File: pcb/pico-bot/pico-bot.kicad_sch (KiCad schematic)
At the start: 2 parts

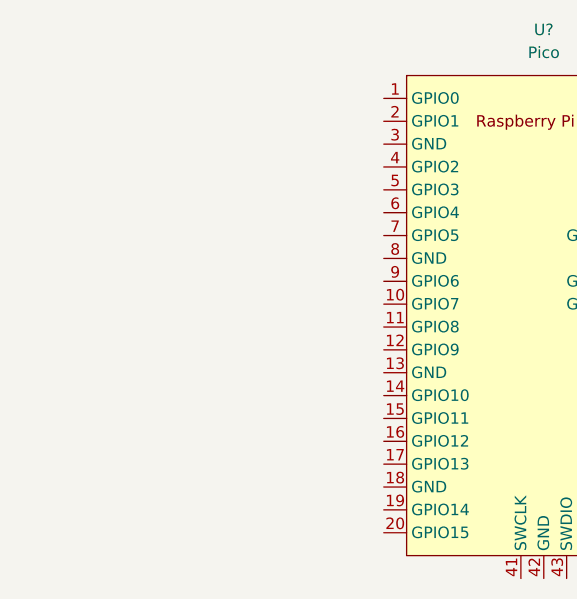
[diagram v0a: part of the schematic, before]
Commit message: Add tb6612fng and mpu6050
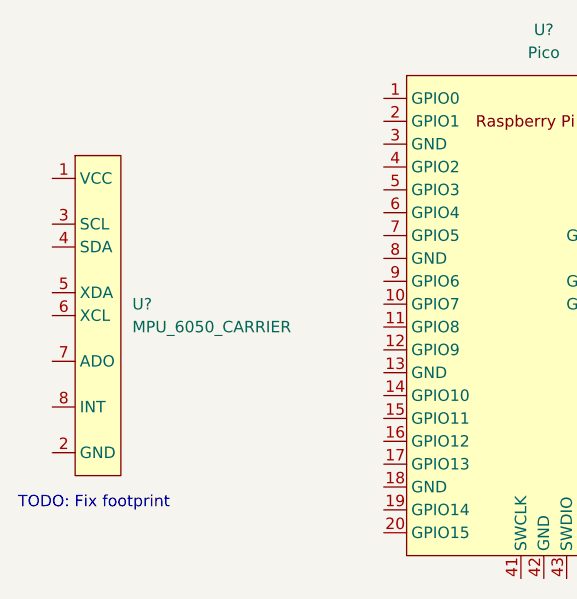
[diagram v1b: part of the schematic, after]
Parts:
- added U?: MPU_6050_CARRIER, symbol pico-bot:MPU_6050_CARRIER
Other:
- note added: "TODO: Fix footprint"
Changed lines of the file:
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@@
 (kicad_sch (version 20211123) (generator eeschema)
   (paper "A4")
+  (text "TODO: Fix footprint" (at 96.52 123.19 0)
+    (effects (font (size 1.27 1.27)) (justify left bottom))
+  )
   (symbol (lib_id "pico-bot:TB6612FNG_DUAL_MOTOR_CARRIER") (at 205.74 87.63 0) (unit 1)
     (in_bom yes) (on_board yes) (fields_autoplaced)
@@
     (pin "8")
     (pin "9")
+  )
+  (symbol (lib_id "pico-bot:MPU_6050_CARRIER") (at 102.87 83.82 0) (unit 1)
+    (in_bom yes) (on_board yes) (fields_autoplaced)
+    (property "Reference" "U?" (id 0) (at 109.22 100.3299 0)
+      (effects (font (size 1.27 1.27)) (justify left))
+    )
+    (property "Value" "MPU_6050_CARRIER" (id 1) (at 109.22 102.8699 0)
+      (effects (font (size 1.27 1.27)) (justify left))
+    )
+    (property "Footprint" "" (id 2) (at 102.87 83.82 0)
+      (effects (font (size 1.27 1.27)) hide)
+    )
+    (property "Datasheet" "" (id 3) (at 102.87 83.82 0)
+      (effects (font (size 1.27 1.27)) hide)
+    )
+    (pin "1")
+    (pin "2")
+    (pin "3")
+    (pin "4")
+    (pin "5")
+    (pin "6")
+    (pin "7")
+    (pin "8")
   )
   (symbol (lib_id "MCU_RaspberryPi_and_Boards:Pico") (at 154.94 101.6 0) (unit 1)
@@
       (reference "U?") (unit 1) (value "TB6612FNG_DUAL_MOTOR_CARRIER") (footprint "pico-bot:TB6612FNG-CARRIER")
     )
+    (path "/a2ae4dd0-6180-48cd-88b8-2d1451b2c40a"
+      (reference "U?") (unit 1) (value "MPU_6050_CARRIER") (footprint "")
+    )
     (path "/c80dc8bc-aa28-4fc2-9632-13f75cbaaee4"

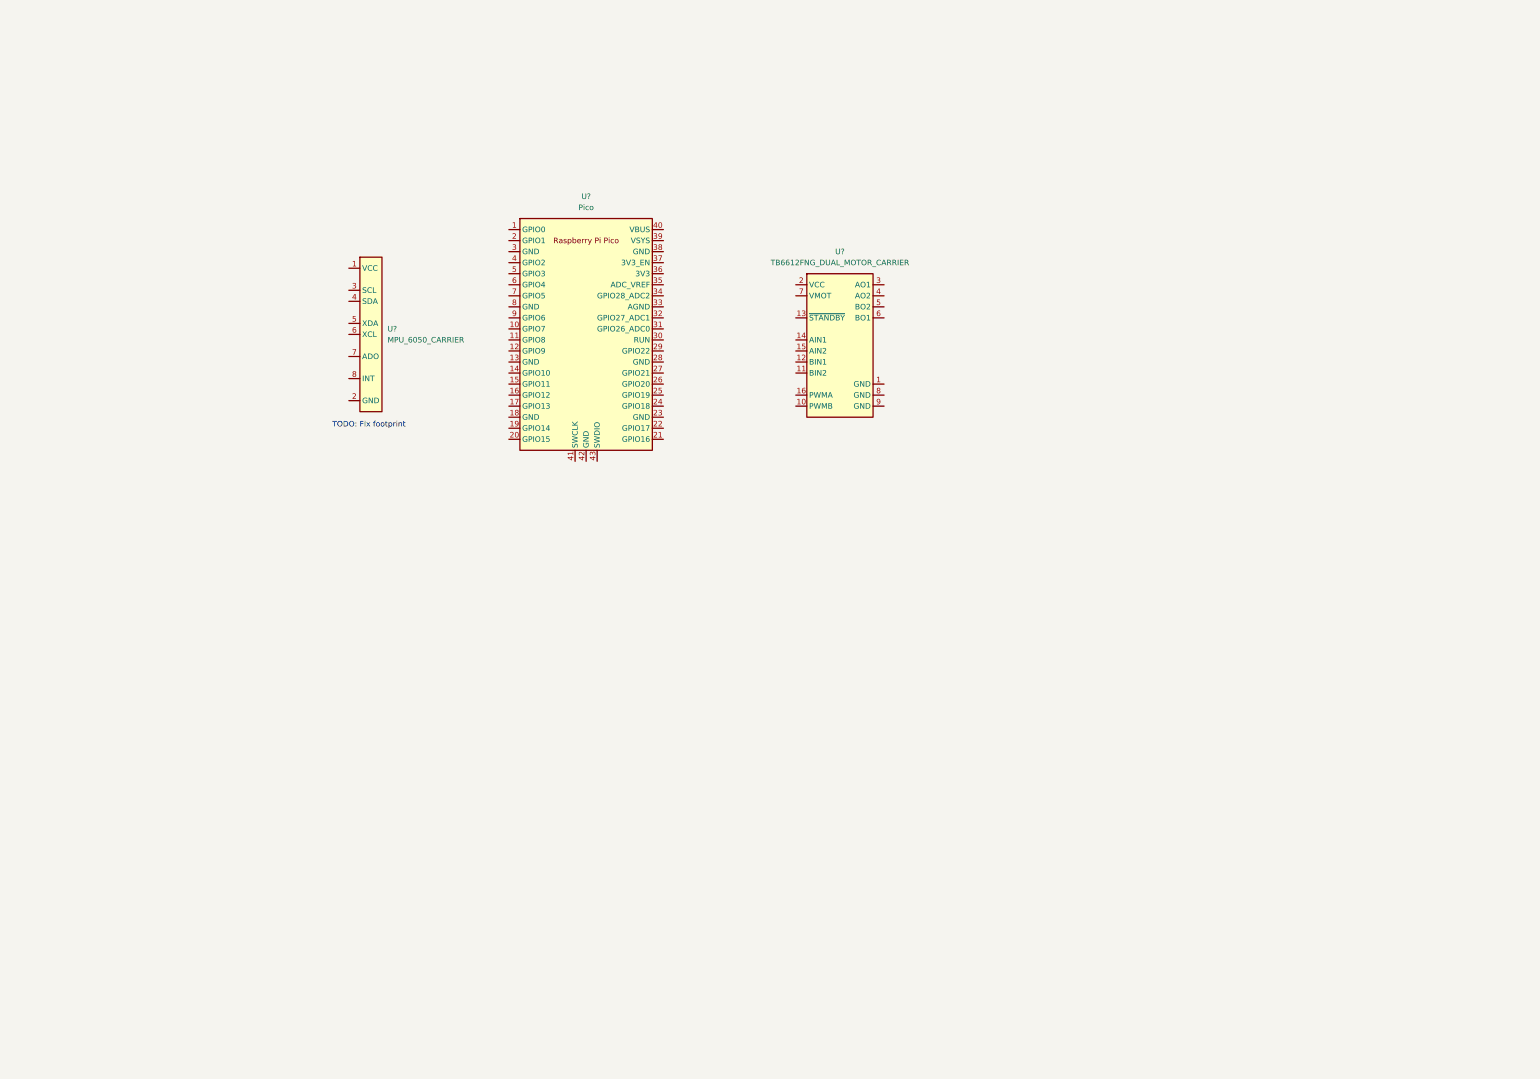
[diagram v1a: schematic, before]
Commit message: Add power circuit up to regulator
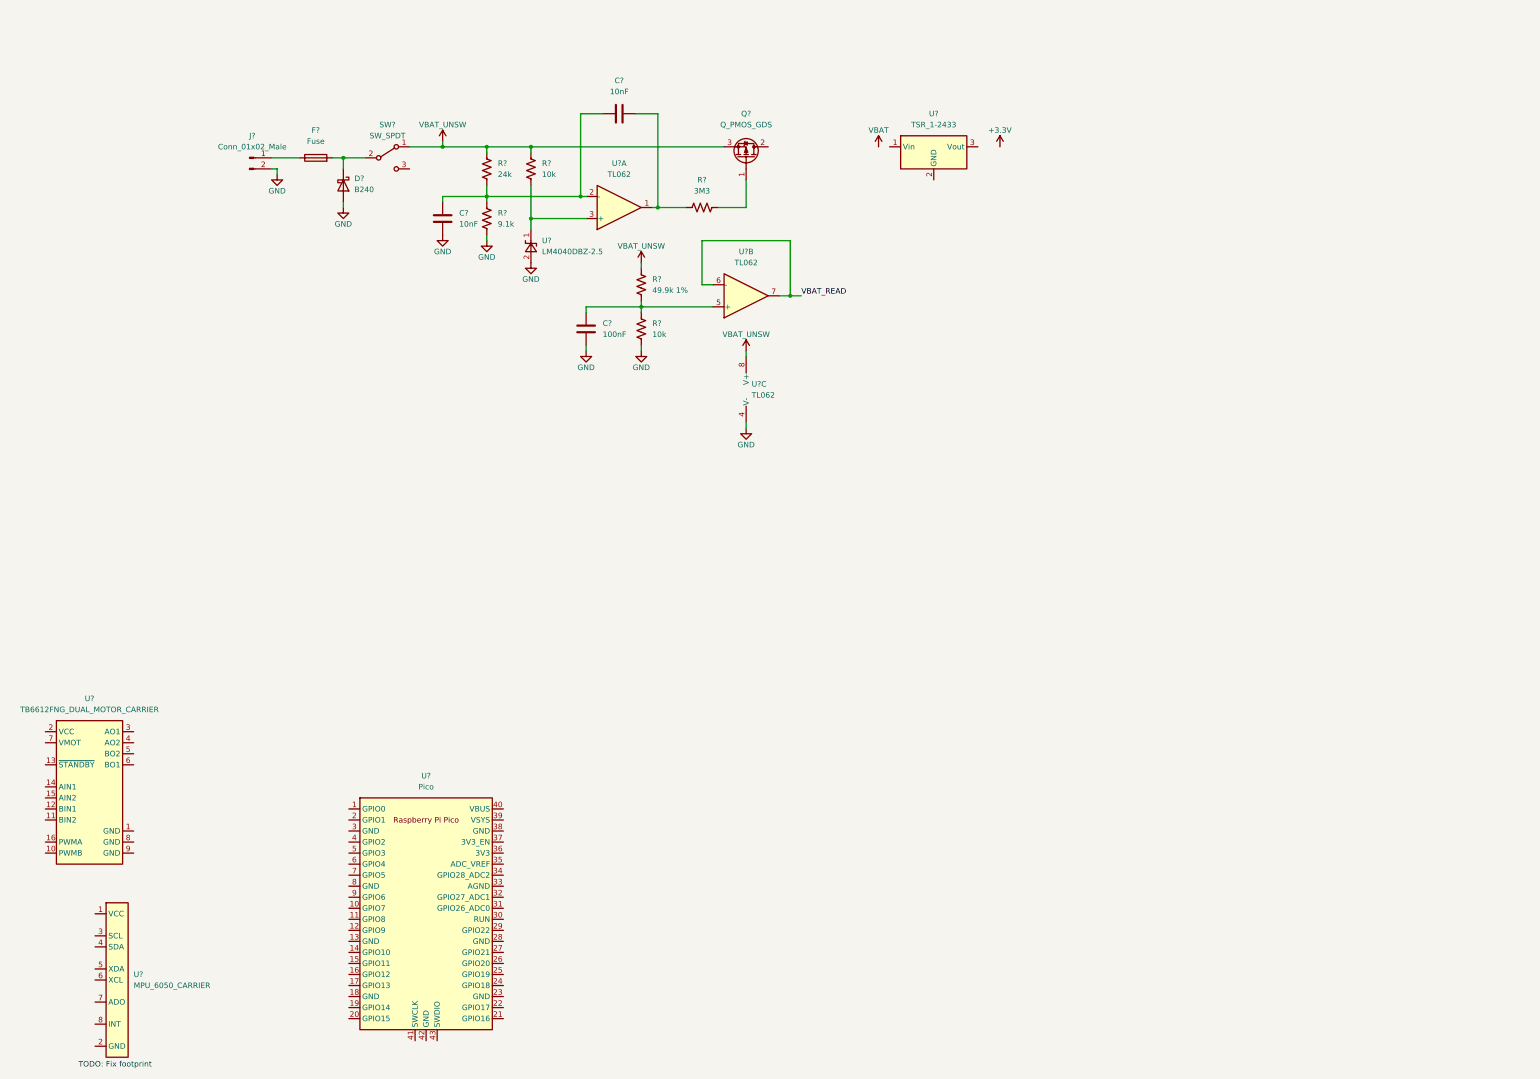
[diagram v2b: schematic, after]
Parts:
- removed U?: Pico, MCU_RaspberryPi_and_Boards:RPi_Pico_SMD_TH, symbol MCU_RaspberryPi_and_Boards:Pico
- added C? (x2): 10nF, Capacitor_SMD:C_0805_2012Metric_Pad1.18x1.45mm_HandSolder, symbol Device:C
- added C?: 100nF, Capacitor_SMD:C_0805_2012Metric_Pad1.18x1.45mm_HandSolder, symbol Device:C
- added D?: B240, Diode_SMD:D_SMB, symbol Diode:B240
- added F?: Fuse, Fuse:Fuseholder_Littelfuse_Nano2_154x, symbol Device:Fuse
- added J?: Conn_01x02_Male, Connector_PinSocket_2.54mm:PinSocket_1x02_P2.54mm_Vertical, symbol Connector:Conn_01x02_Male
- added Q?: Q_PMOS_GDS, symbol Device:Q_PMOS_GDS
- added R?: 9.1k, Resistor_SMD:R_0805_2012Metric_Pad1.20x1.40mm_HandSolder, symbol Device:R_US
- added R? (x2): 10k, Resistor_SMD:R_0805_2012Metric_Pad1.20x1.40mm_HandSolder, symbol Device:R_US
- added R?: 3M3, Resistor_SMD:R_0805_2012Metric_Pad1.20x1.40mm_HandSolder, symbol Device:R_US
- added R?: 49.9k 1%, Resistor_SMD:R_0805_2012Metric_Pad1.20x1.40mm_HandSolder, symbol Device:R_US
- added R?: 24k, Resistor_SMD:R_0805_2012Metric_Pad1.20x1.40mm_HandSolder, symbol Device:R_US
- added SW?: SW_SPDT, symbol Switch:SW_SPDT
- added U? (x2): TL062, symbol Amplifier_Operational:TL062
- added U?: LM4040DBZ-2.5, Package_TO_SOT_SMD:SOT-23, symbol Reference_Voltage:LM4040DBZ-2.5
- added U?: TSR_1-2433, Converter_DCDC:Converter_DCDC_TRACO_TSR-1_THT, symbol Regulator_Switching:TSR_1-2433
- added U?: Pico, RPi_Pico:RPi_Pico_SMD_TH, symbol MCU_RaspberryPi_and_Boards:Pico
- added U?: TL062, Package_SO:SOIC-8-1EP_3.9x4.9mm_P1.27mm_EP2.29x3mm, symbol Amplifier_Operational:TL062
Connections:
- new net: D?.1 (K), F?.2, SW?.2 (B)
- new net: C?.2, R?.1, R?.2, U?.5 (+)
- new net: C?.1, C?.2, R?.1, R?.2, U?.2 (-)
- new net: R?.1, U?.1 (K), U?.3 (+)
- new net: F?.1, J?.1 (Pin_1)
- new net: C?.2, R?.1, U?.1
- new net: Q?.1 (G), R?.2
- new net GND: C?.1, C?.1, D?.2 (A), J?.2 (Pin_2), R?.1, R?.1, U?.2 (A), U?.4 (V-)
- new net VBAT_READ: U?.6 (-), U?.7
- new net VBAT_UNSW: Q?.3 (S), R?.2, R?.2, R?.2, SW?.1 (A), U?.8 (V+)
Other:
- moved on the sheet: U?

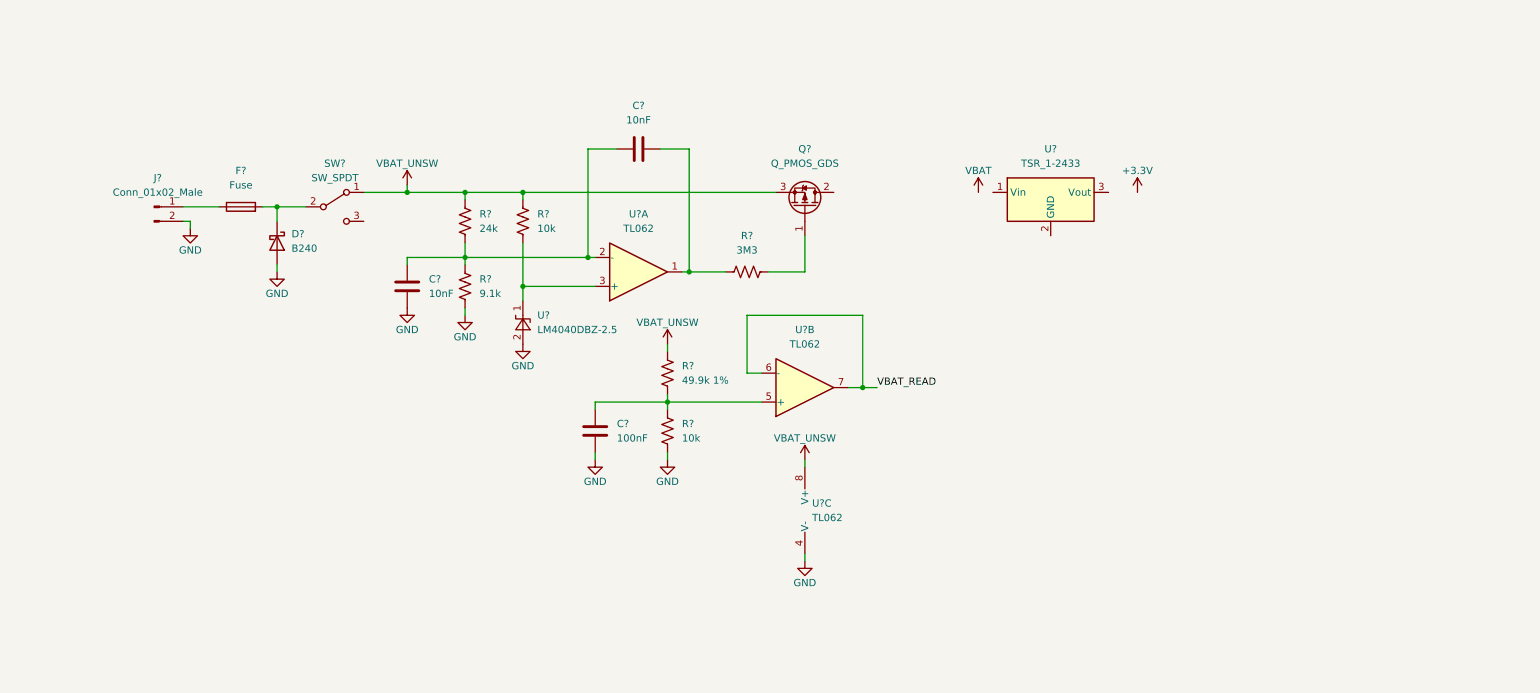
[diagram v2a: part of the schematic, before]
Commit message: Finish power circuit
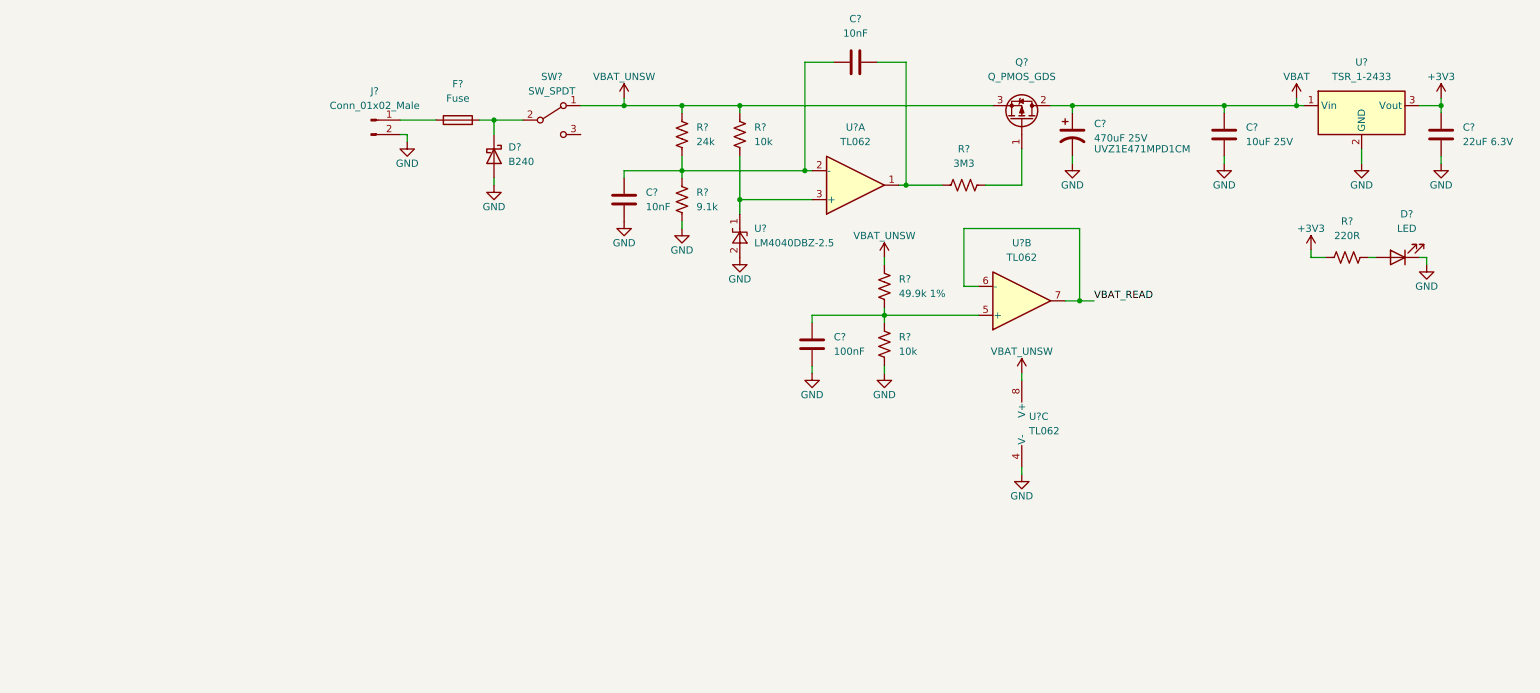
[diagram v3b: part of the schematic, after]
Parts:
- added C?: 22uF 6.3V, Capacitor_SMD:C_0805_2012Metric_Pad1.18x1.45mm_HandSolder, symbol Device:C
- added C?: 470uF 25V, Capacitor_THT:CP_Radial_D10.0mm_P5.00mm, symbol Device:C_Polarized_US
- added C?: 10uF 25V, Capacitor_SMD:C_1206_3216Metric_Pad1.33x1.80mm_HandSolder, symbol Device:C
- added D?: LED, LED_SMD:LED_0805_2012Metric_Pad1.15x1.40mm_HandSolder, symbol Device:LED
- added R?: 220R, Resistor_SMD:R_0805_2012Metric_Pad1.20x1.40mm_HandSolder, symbol Device:R_US
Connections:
- net +3V3: now also U?.3 (Vout), C?.2, R?.1
- net GND: now also U?.2 (GND), C?.1, C?.1, C?.2, D?.1 (K)
- net VBAT: now also Q?.2 (D), U?.1 (Vin), C?.1, C?.2
- new net: D?.2 (A), R?.2
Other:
- moved on the sheet: C?, D?, F?, J?, Q?, R?, SW?, U?, U?A, U?B, U?C
